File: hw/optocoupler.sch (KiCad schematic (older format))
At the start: 2 parts

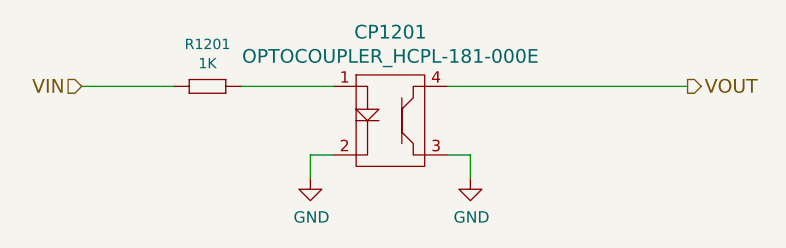
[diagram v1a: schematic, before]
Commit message: radio & aux are on when ign key is on
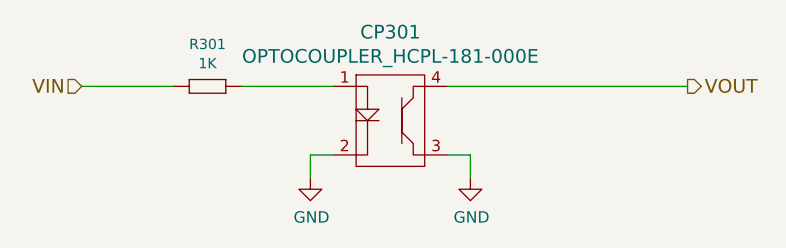
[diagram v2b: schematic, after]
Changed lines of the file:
@@
 EESchema Schematic File Version 2
 LIBS:kemet
-LIBS:multicomp
 LIBS:power
 LIBS:usevolt
 LIBS:wurth_elektronik_LED
+LIBS:yageo
 LIBS:fsb-cache
 EELAYER 26 0
@@
 $Descr A4 11693 8268
 encoding utf-8
-Sheet 12 12
+Sheet 3 9
 Title ""
 Date ""
@@
 AR Path="/59C3566B/58998C01" Ref="R1102"  Part="1"
 AR Path="/59C35BD6/58998C01" Ref="R1201"  Part="1"
-F 0 "R1201" H 3850 3184 45  0000 C CNN
+AR Path="/595401A8/59C2BC93/58998C01" Ref="R301"  Part="1"
+F 0 "R301" H 3850 3184 45  0000 C CNN
 F 1 "1K" H 3850 3100 45  0000 C CNN
 F 2 "multicomp:0603" H 3830 3150 20  0001 C CNN
@@
 $EndComp
 $Comp
-L GND #PWR042
+L GND #PWR043
 U 1 1 58998C09
 P 4300 3400
-AR Path="/59C3380F/58998C09" Ref="#PWR042"  Part="1"
-AR Path="/59C34D8B/58998C09" Ref="#PWR044"  Part="1"
-AR Path="/59C3566B/58998C09" Ref="#PWR046"  Part="1"
-AR Path="/59C35BD6/58998C09" Ref="#PWR048"  Part="1"
-F 0 "#PWR048" H 4300 3150 50  0001 C CNN
+AR Path="/59C3380F/58998C09" Ref="#PWR043"  Part="1"
+AR Path="/59C34D8B/58998C09" Ref="#PWR045"  Part="1"
+AR Path="/59C3566B/58998C09" Ref="#PWR047"  Part="1"
+AR Path="/59C35BD6/58998C09" Ref="#PWR049"  Part="1"
+AR Path="/595401A8/59C2BC93/58998C09" Ref="#PWR016"  Part="1"
+F 0 "#PWR016" H 4300 3150 50  0001 C CNN
 F 1 "GND" H 4305 3227 50  0000 C CNN
 F 2 "" H 4300 3400 50  0000 C CNN
@@
 $EndComp
 $Comp
-L GND #PWR043
+L GND #PWR044
 U 1 1 58998C1A
 P 5000 3400
-AR Path="/59C3380F/58998C1A" Ref="#PWR043"  Part="1"
-AR Path="/59C34D8B/58998C1A" Ref="#PWR045"  Part="1"
-AR Path="/59C3566B/58998C1A" Ref="#PWR047"  Part="1"
-AR Path="/59C35BD6/58998C1A" Ref="#PWR049"  Part="1"
-F 0 "#PWR049" H 5000 3150 50  0001 C CNN
+AR Path="/59C3380F/58998C1A" Ref="#PWR044"  Part="1"
+AR Path="/59C34D8B/58998C1A" Ref="#PWR046"  Part="1"
+AR Path="/59C3566B/58998C1A" Ref="#PWR048"  Part="1"
+AR Path="/59C35BD6/58998C1A" Ref="#PWR050"  Part="1"
+AR Path="/595401A8/59C2BC93/58998C1A" Ref="#PWR017"  Part="1"
+F 0 "#PWR017" H 5000 3150 50  0001 C CNN
 F 1 "GND" H 5005 3227 50  0000 C CNN
 F 2 "" H 5000 3400 50  0000 C CNN
@@
 AR Path="/59C3566B/597BAFD2" Ref="CP1101"  Part="1"
 AR Path="/59C35BD6/597BAFD2" Ref="CP1201"  Part="1"
-F 0 "CP1201" H 4650 3437 60  0000 C CNN
+AR Path="/595401A8/59C2BC93/597BAFD2" Ref="CP301"  Part="1"
+F 0 "CP301" H 4650 3437 60  0000 C CNN
 F 1 "OPTOCOUPLER_HCPL-181-000E" H 4650 3331 60  0000 C CNN
 F 2 "usevolt:HCPL-181-000E" H 4600 3300 60  0001 C CNN
